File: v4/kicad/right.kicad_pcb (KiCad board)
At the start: 2 copper layers, 158 x 119 mm, 72 parts

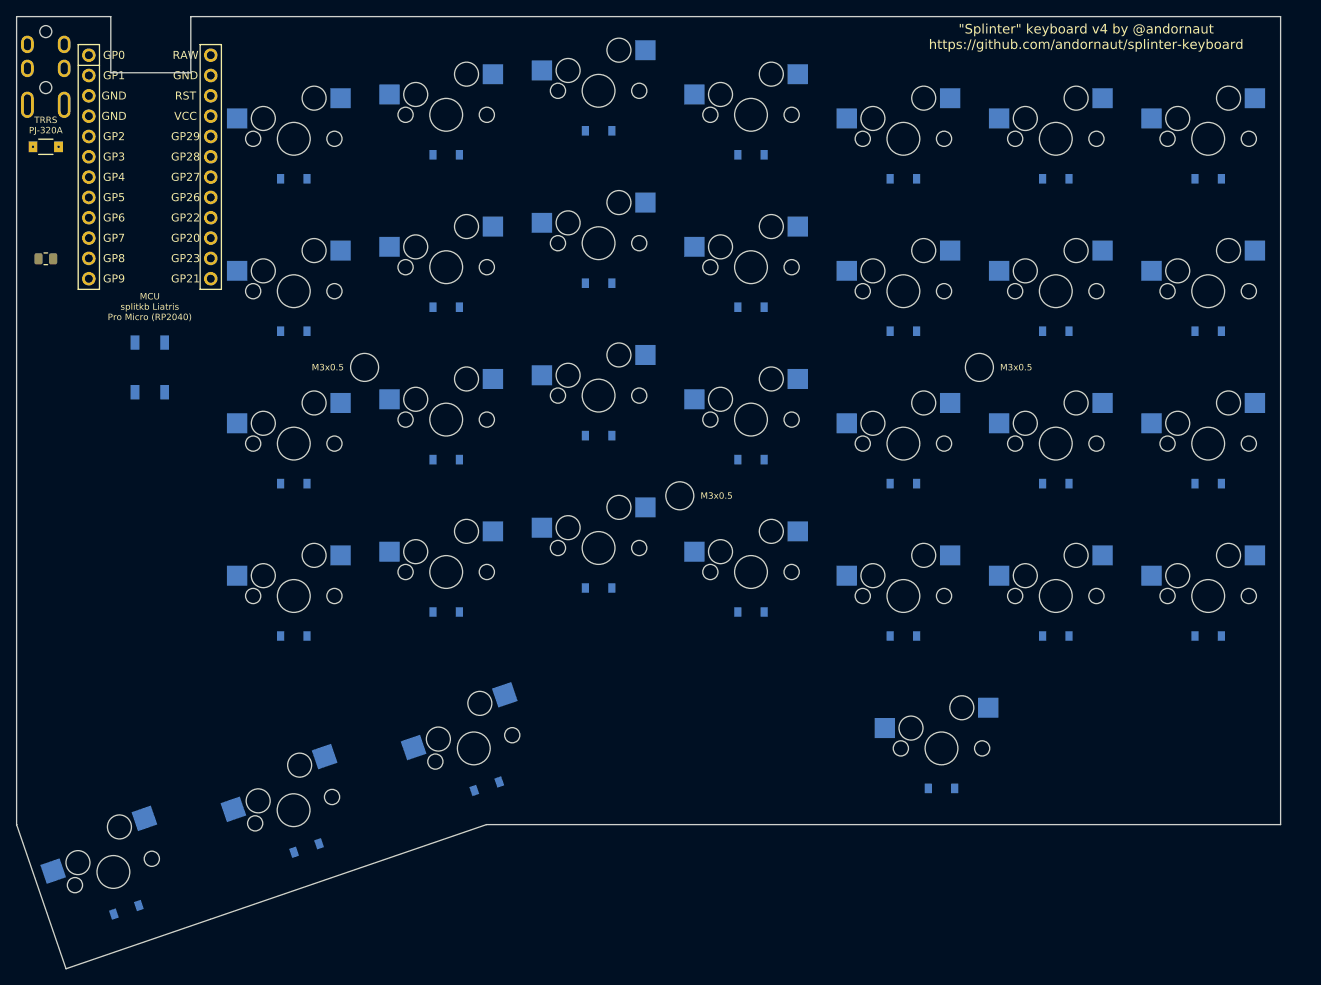
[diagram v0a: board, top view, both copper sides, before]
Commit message: v4: SMD footprints with both-side routing vias; mute pcbnew noise
Footprints:
- Add r_0805 (single-side 0805 SMD) and convert sod-123fl from reversible
  THT to single-side SMD; both gain an opt-in include_traces_vias helper
  (via just outside each pad) plus a via_in_pad option (via in the pad,
  needs filled-and-capped vias for reflow, off by default).
- config.yaml: data_resistor switched infused-kim/smd_0805 -> r_0805,
  data_tvs + data_resistor get include_traces_vias for both-side routing,
  and the matrix diode gets reversible + include_traces_vias so its net
  routes on either layer (single-side assembly unchanged).

Tooling:
- lib.sh mute_pcbnew_noise helper drops KiCad's harmless PROPERTY_ENUM
  wxASSERT from stderr; applied in build/copy scripts, and autoroute.py
  silences the same noise around its in-process pcbnew import.
- gen-jlcpcb-bom-cpl.py groups Do-Not-Place footprints by package and
  reports them so an unintended DNP is visible.

Docs: refresh README and v4/README; register r_0805 in the Dockerfile.
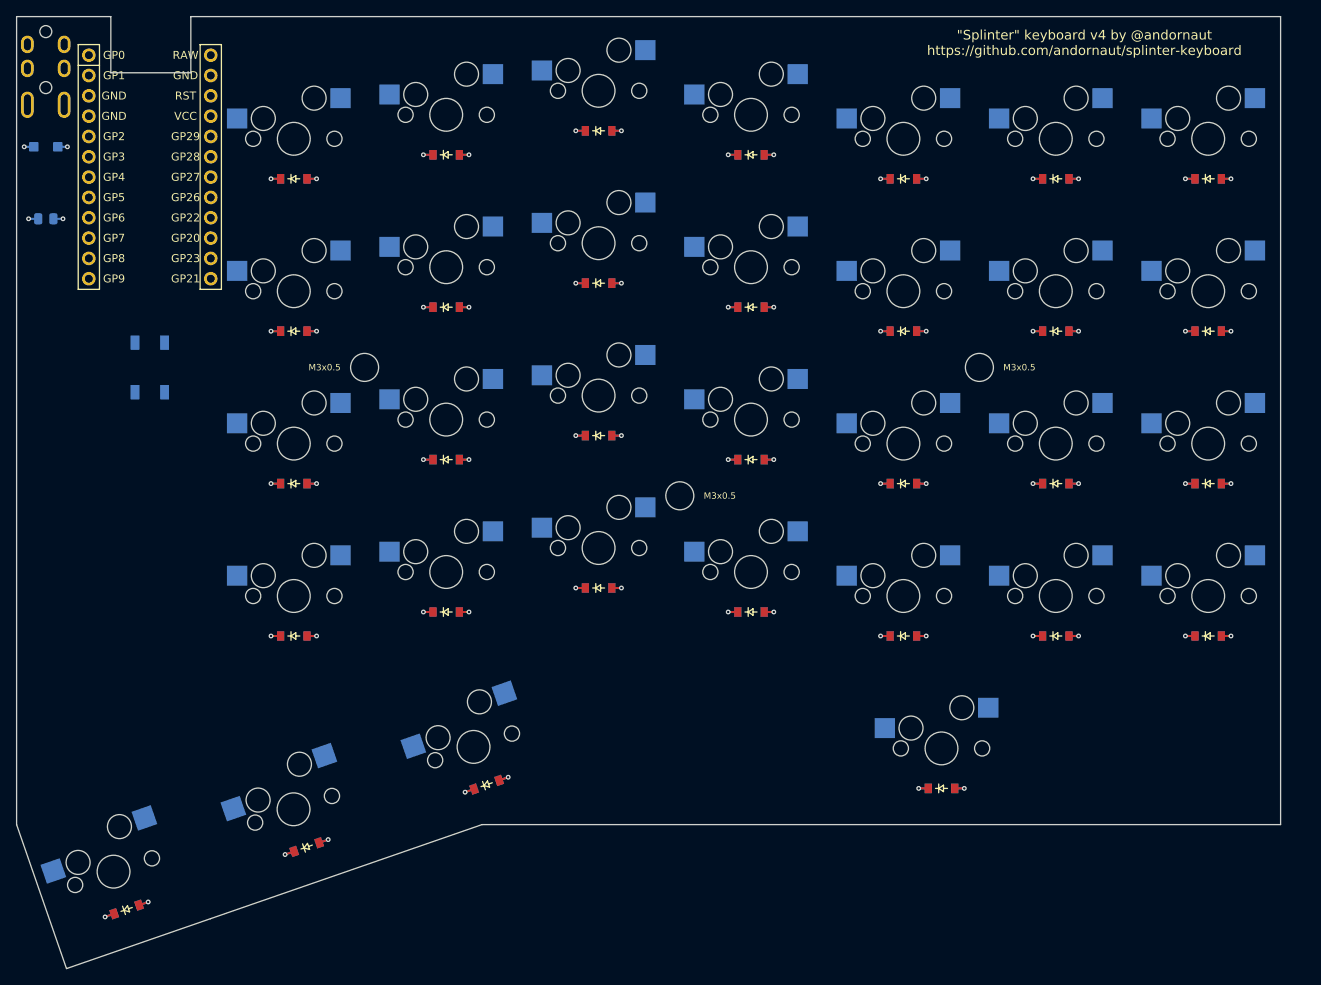
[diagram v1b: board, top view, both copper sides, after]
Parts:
- D1, D10, D11, D12, D13, D14, D15, D16, D17, D18, D19, D2, D20, D21, D22, D23, D24, D25, D26, D27, D28, D29, D3, D30, D31, D32, D4, D5, D6, D7, D8, D9: moved to F.Cu
- D33: footprint splinter:D_SOD-123FL_HandSolder -> splinter:D_SOD-123FL; moved to B.Cu
- R1: value (none) -> 100R; footprint smd_805 -> splinter:R_0805; moved to B.Cu
- moved R1 5.00 mm to (134.5, 113.8)
- moved D30 0.19 mm to (189.6, 184.5), turned to 19.1117 degrees
- moved S30 0.19 mm to (188.0, 179.8), turned to 19.1117 degrees
- moved D31 0.12 mm to (167.1, 192.3), turned to 19.1117 degrees
- moved S31 0.11 mm to (165.5, 187.6), turned to 19.1117 degrees
- moved D32 0.06 mm to (144.6, 200.1), turned to 19.1117 degrees
- turned S32 to 19.1117 degrees
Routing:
- net P16: track 0.00 -> 16.8 mm, vias 0 -> 7
- net P15: track 0.00 -> 16.8 mm, vias 0 -> 7
- net P14: track 0.00 -> 16.8 mm, vias 0 -> 7
- net P10: track 0.00 -> 16.8 mm, vias 0 -> 7
- net P9: track 0.00 -> 9.60 mm, vias 0 -> 4
- net dash_upper: track 0.00 -> 2.40 mm, vias 0 -> 1
- net dash_num: track 0.00 -> 2.40 mm, vias 0 -> 1
- net dash_lower: track 0.00 -> 2.40 mm, vias 0 -> 1
- net dash_home: track 0.00 -> 2.40 mm, vias 0 -> 1
- net zero_upper: track 0.00 -> 2.40 mm, vias 0 -> 1
- net zero_num: track 0.00 -> 2.40 mm, vias 0 -> 1
- net zero_lower: track 0.00 -> 2.40 mm, vias 0 -> 1
- net zero_home: track 0.00 -> 2.40 mm, vias 0 -> 1
- net mirror_four_upper: track 0.00 -> 2.40 mm, vias 0 -> 1
- net mirror_four_num: track 0.00 -> 2.40 mm, vias 0 -> 1
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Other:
- outline, holes or cut-outs redrawn

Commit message: v4: fork SOD-123 diode footprint, counter-rotate thumb diodes; add OK success lines to scripts
Switch v4 matrix/thumb diodes from ceoloide/diode_tht_sod123 to the forked
diode_sod123 footprint (matched where: regex per key group). Thumb diodes
counter-rotate by -thumb_splay to sit horizontal, with a thumb_diode_dx nudge
to re-center under the splayed switch; both driven by single-source-of-truth
units. Re-key jlcpcb-parts.json to diode_sod123 and set rotation 180 so the
cathode band lands on pad 1 in JLC DFM.

Register diode_sod123 in the Dockerfile GUI image (sed loop over footprint
stems). Add a uniform ok() helper in lib.sh and a trailing OK: success line to
each script wrapper. Regenerate left/right PCBs (working and routed).
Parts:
- D1, D10, D11, D12, D13, D14, D15, D16, D17, D18, D19, D2, D20, D21, D22, D23, D24, D25, D26, D27, D28, D29, D3, D30, D31, D32, D4, D5, D6, D7, D8, D9: footprint ceoloide:diode_tht_sod123 -> splinter:diode_sod123; moved to B.Cu
- moved D31 1.73 mm to (165.5, 192.9), turned to 0 degrees
- moved D32 1.73 mm to (143.0, 200.7), turned to 0 degrees
- moved D30 1.73 mm to (188.0, 185.1), turned to 0 degrees

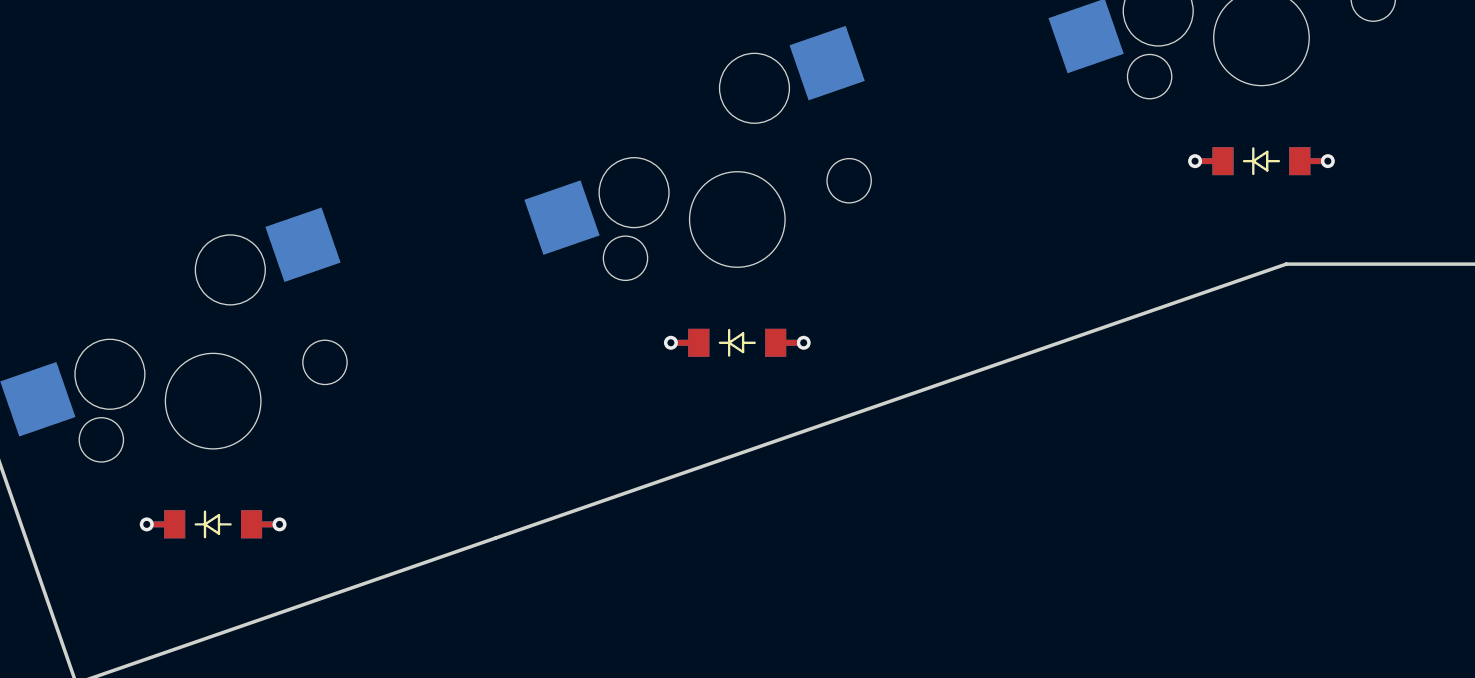
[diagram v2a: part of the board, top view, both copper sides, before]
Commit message: v4: parameterize thumb diode offset, center under switch
Add thumb_diode_dy/dx units for the horizontal thumb diodes' offset from
their splayed switches. dx re-centers laterally (the rotated dy would drift
it sideways); keep dx = dy * tan(thumb_splay) so it stays centered when dy
changes, and dx auto-flips x on the mirrored right half. Set dy to -4.7
(sits ~4.97mm below the switch, level with the matrix diodes), centered.
Regenerate both halves and the routed copies.
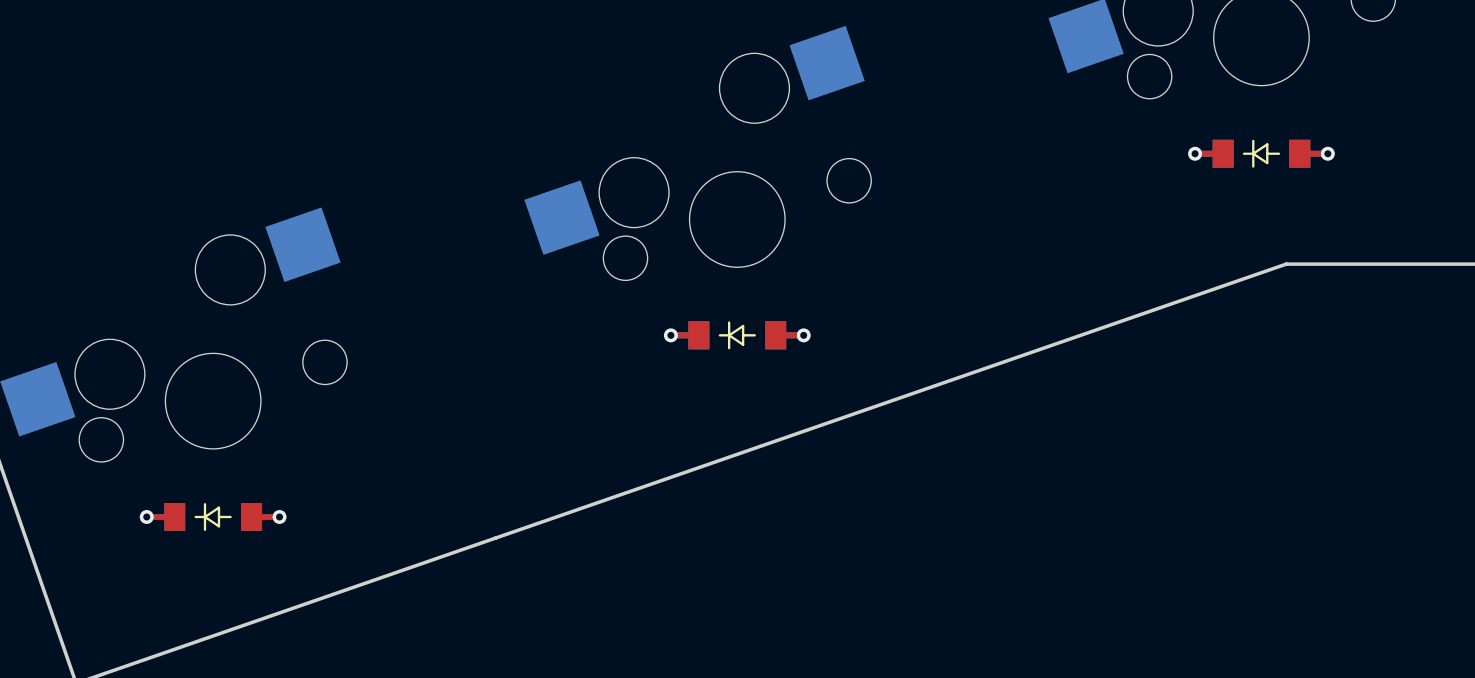
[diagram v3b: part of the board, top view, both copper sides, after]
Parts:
- moved D32 0.32 mm to (143.0, 200.4)
- moved D30 0.32 mm to (188.0, 184.8)
- moved D31 0.32 mm to (165.5, 192.6)
